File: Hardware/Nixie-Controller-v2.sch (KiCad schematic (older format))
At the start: 219 parts, among them J7 12V DC JACK, U1 MAX1771, U10 74HC4067, U11 M41T01, U12 STM32F103C8, U13 OPA180, U14 74HC4067, U15 OPA180, U16 74HC4067, U17 OPA180, U18 74HC4067, U19 OPA180, U2 BH2226, U20 74HC4067, U21 OPA180, U22 74HC4067, U3 74HC595, U4 74HC595, U5 74HC595, U6 SN74LVCC3245A, U7 NCP1117-5.0, U8 NCP1117-3.3, U9 OPA180, Y1 32.768KHz, Y2 16MHz

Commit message: Remove uC external crystal
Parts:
- removed C24, C25: 10pF, Capacitor_SMD:C_0402_1005Metric, symbol Device:C_Small
- removed Y2: 16MHz, Crystal:Crystal_SMD_2016-4Pin_2.0x1.6mm, symbol Device:Crystal_GND24
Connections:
- wire segments 618 -> 608
- no-connect marks 66 -> 68
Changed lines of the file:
@@
 	0    -1   -1   0
 $EndComp
-Wire Wire Line
-	18050 9850 19300 9850
-Wire Wire Line
-	18050 9750 19300 9750
 $Comp
 L Device:R_Small_US R28
@@
 	1    18850 9200
 	-1   0    0    1
-$EndComp
-$Comp
-L power:GND #PWR0131
-U 1 1 6186A334
-P 20000 10350
-F 0 "#PWR0131" H 20000 10100 50  0001 C CNN
-F 1 "GND" H 20000 10200 50  0000 C CNN
-F 2 "" H 20000 10350 50  0001 C CNN
-F 3 "" H 20000 10350 50  0001 C CNN
-	1    20000 10350
-	1    0    0    -1
-$EndComp
-$Comp
-L power:GND #PWR0125
-U 1 1 61866ACC
-P 20000 9250
-F 0 "#PWR0125" H 20000 9000 50  0001 C CNN
-F 1 "GND" H 20000 9100 50  0000 C CNN
-F 2 "" H 20000 9250 50  0001 C CNN
-F 3 "" H 20000 9250 50  0001 C CNN
-	1    20000 9250
-	-1   0    0    1
-$EndComp
-$Comp
-L power:GND #PWR0129
-U 1 1 618618D6
-P 20200 9800
-F 0 "#PWR0129" H 20200 9550 50  0001 C CNN
-F 1 "GND" V 20200 9650 50  0000 R CNN
-F 2 "" H 20200 9800 50  0001 C CNN
-F 3 "" H 20200 9800 50  0001 C CNN
-	1    20200 9800
-	0    -1   -1   0
-$EndComp
-$Comp
-L power:GND #PWR0128
-U 1 1 6185E39D
-P 19800 9800
-F 0 "#PWR0128" H 19800 9550 50  0001 C CNN
-F 1 "GND" V 19800 9650 50  0000 R CNN
-F 2 "" H 19800 9800 50  0001 C CNN
-F 3 "" H 19800 9800 50  0001 C CNN
-	1    19800 9800
-	0    1    1    0
-$EndComp
-Connection ~ 20000 10050
-Wire Wire Line
-	20000 10050 20000 10150
-Wire Wire Line
-	20000 10050 20000 9950
-Wire Wire Line
-	19300 10050 20000 10050
-Wire Wire Line
-	19300 9850 19300 10050
-Wire Wire Line
-	20000 9550 20000 9650
-Connection ~ 20000 9550
-Wire Wire Line
-	19300 9550 19300 9750
-Wire Wire Line
-	20000 9550 19300 9550
-Wire Wire Line
-	20000 9450 20000 9550
-$Comp
-L Device:C_Small C25
-U 1 1 6169E719
-P 20000 10250
-F 0 "C25" H 20100 10300 50  0000 L CNN
-F 1 "10pF" H 20100 10200 50  0000 L CNN
-F 2 "Capacitor_SMD:C_0402_1005Metric" H 20000 10250 50  0001 C CNN
-F 3 "~" H 20000 10250 50  0001 C CNN
-F 4 "Yageo" H 20000 10250 50  0001 C CNN "Manufacturer"
-F 5 "CC0402CRNPO9BN100" H 20000 10250 50  0001 C CNN "Part#"
-	1    20000 10250
-	1    0    0    -1
-$EndComp
-$Comp
-L Device:C_Small C24
-U 1 1 6169D2AB
-P 20000 9350
-F 0 "C24" H 20100 9400 50  0000 L CNN
-F 1 "10pF" H 20100 9300 50  0000 L CNN
-F 2 "Capacitor_SMD:C_0402_1005Metric" H 20000 9350 50  0001 C CNN
-F 3 "~" H 20000 9350 50  0001 C CNN
-F 4 "Yageo" H 20000 9350 50  0001 C CNN "Manufacturer"
-F 5 "CC0402CRNPO9BN100" H 20000 9350 50  0001 C CNN "Part#"
-	1    20000 9350
-	1    0    0    -1
-$EndComp
-$Comp
-L Device:Crystal_GND24 Y2
-U 1 1 6163FF36
-P 20000 9800
-F 0 "Y2" V 19750 10000 50  0000 L CNN
-F 1 "16MHz" V 19850 9900 50  0000 L CNN
-F 2 "Crystal:Crystal_SMD_2016-4Pin_2.0x1.6mm" H 20000 9800 50  0001 C CNN
-F 3 "~" H 20000 9800 50  0001 C CNN
-F 4 "ECS" H 20000 9800 50  0001 C CNN "Manufacturer"
-F 5 "ECS-160-8-37-CWY-TR" H 20000 9800 50  0001 C CNN "Part#"
-	1    20000 9800
-	0    1    1    0
 $EndComp
 Wire Wire Line
@@
 	1    0    0    -1
 $EndComp
+NoConn ~ 18050 9750
+NoConn ~ 18050 9850
 $EndSCHEMATC

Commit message: Fix Q2~Q61 footprint (schematic only)
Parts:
- removed Q10, Q11, Q12, Q13, Q14, Q15, Q16, Q17, Q18, Q19, Q2, Q20, Q21, Q22, Q23, Q24, Q25, Q26, Q27, Q28, Q29, Q3, Q30, Q31, Q32, Q33, Q34, Q35, Q36, Q37, Q38, Q39, Q4, Q40, Q41, Q42, Q43, Q44, Q45, Q46, Q47, Q48, Q49, Q5, Q50, Q51, Q52, Q53, Q54, Q55, Q56, Q57, Q58, Q59, Q6, Q60, Q61, Q7, Q8, Q9: ~, Package_TO_SOT_SMD:SOT-23, symbol Device:Q_NPN_EBC
- added Q10, Q11, Q12, Q13, Q14, Q15, Q16, Q17, Q18, Q19, Q2, Q20, Q21, Q22, Q23, Q24, Q25, Q26, Q27, Q28, Q29, Q3, Q30, Q31, Q32, Q33, Q34, Q35, Q36, Q37, Q38, Q39, Q4, Q40, Q41, Q42, Q43, Q44, Q45, Q46, Q47, Q48, Q49, Q5, Q50, Q51, Q52, Q53, Q54, Q55, Q56, Q57, Q58, Q59, Q6, Q60, Q61, Q7, Q8, Q9: ~, Package_TO_SOT_SMD:SOT-23, symbol Device:Q_NPN_BEC

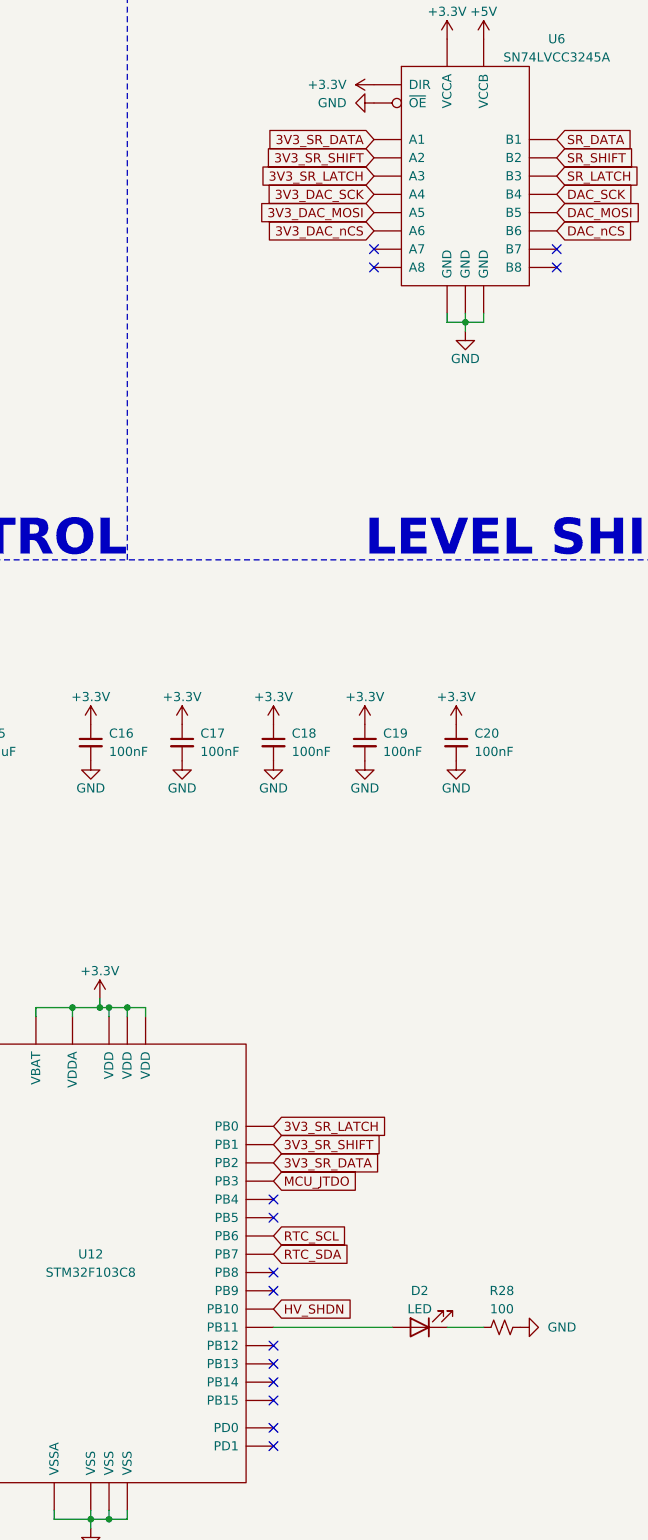
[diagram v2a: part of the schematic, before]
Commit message: Connect shift register to SPI ports
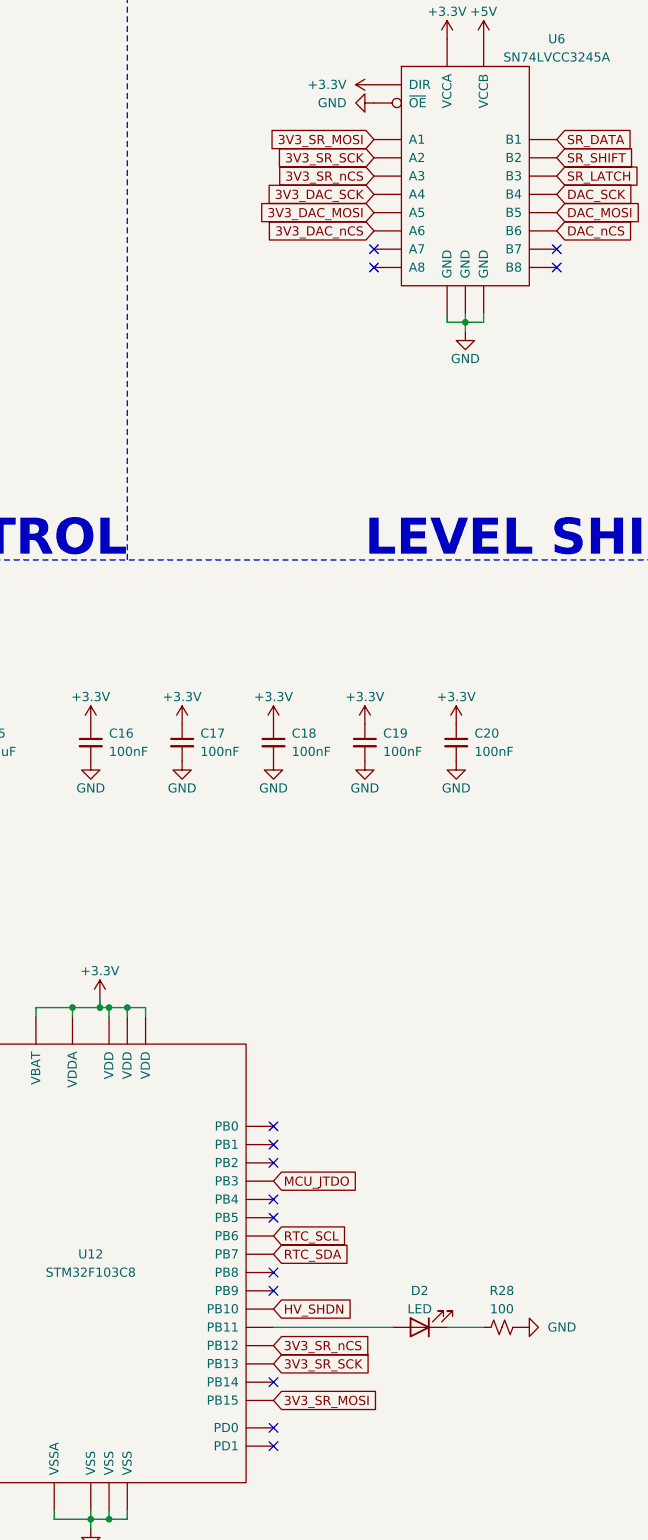
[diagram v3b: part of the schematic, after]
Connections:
- net 3V3_SR_nCS: now reaches U12.25 (PB12)
- net 3V3_SR_nCS: now also U6.5 (A3)
- net 3V3_SR_SCK: now reaches U12.26 (PB13)
- net 3V3_SR_SCK: now also U6.4 (A2)
- net 3V3_SR_MOSI: now reaches U12.28 (PB15)
- net 3V3_SR_MOSI: now also U6.3 (A1)
- net 3V3_SR_DATA: no longer names the net of U12.20 (PB2)
- net 3V3_SR_DATA: no longer U6.3 (A1)
- net 3V3_SR_LATCH: no longer names the net of U12.18 (PB0)
- net 3V3_SR_LATCH: no longer U6.5 (A3)
- net 3V3_SR_SHIFT: no longer names the net of U12.19 (PB1)
- net 3V3_SR_SHIFT: no longer U6.4 (A2)
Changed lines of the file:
@@
 	1    0    0    -1
 $EndComp
-Text GLabel 18600 2800 0    50   Input ~ 0
-3V3_SR_SHIFT
-Text GLabel 18600 2900 0    50   Input ~ 0
-3V3_SR_LATCH
-Text GLabel 18600 2700 0    50   Input ~ 0
-3V3_SR_DATA
 Text GLabel 18600 3000 0    50   Input ~ 0
 3V3_DAC_SCK
@@
 Text GLabel 16050 7900 0    50   Input ~ 0
 MCU_nRST
-$Comp
-L Nixie-Controller-v2:STM32F103C8 U12
-U 1 1 6163BD96
-P 17050 8850
-F 0 "U12" H 17050 8900 50  0000 C CNN
-F 1 "STM32F103C8" H 17050 8800 50  0000 C CNN
-F 2 "Package_QFP:LQFP-48_7x7mm_P0.5mm" H 17050 8900 50  0001 C CNN
-F 3 "~" H 17050 8900 50  0001 C CNN
-F 4 "ST Micro" H 17050 8850 50  0001 C CNN "Manufacturer"
-F 5 "STM32F103C8T6" H 17050 8850 50  0001 C CNN "Part#"
-	1    17050 8850
-	1    0    0    -1
-$EndComp
 Text GLabel 16050 8500 0    50   Input ~ 0
 3V3_DAC_nCS
@@
 Text GLabel 16050 8600 0    50   Input ~ 0
 3V3_DAC_SCK
-Text GLabel 18050 8300 2    50   Input ~ 0
-3V3_SR_DATA
-Text GLabel 18050 8100 2    50   Input ~ 0
-3V3_SR_LATCH
-Text GLabel 18050 8200 2    50   Input ~ 0
-3V3_SR_SHIFT
+Text GLabel 18050 9600 2    50   Input ~ 0
+3V3_SR_MOSI
+Text GLabel 18050 9300 2    50   Input ~ 0
+3V3_SR_nCS
+Text GLabel 18050 9400 2    50   Input ~ 0
+3V3_SR_SCK
 Text GLabel 18050 9100 2    50   Input ~ 0
 HV_SHDN
@@
 NoConn ~ 16050 9850
 NoConn ~ 16050 9950
-NoConn ~ 18050 9600
 NoConn ~ 18050 9500
-NoConn ~ 18050 9400
-NoConn ~ 18050 9300
 NoConn ~ 18050 9000
 NoConn ~ 18050 8900
@@
 	1    0    0    -1
 $EndComp
+Text GLabel 18600 2700 0    50   Input ~ 0
+3V3_SR_MOSI
+Text GLabel 18600 2900 0    50   Input ~ 0
+3V3_SR_nCS
+Text GLabel 18600 2800 0    50   Input ~ 0
+3V3_SR_SCK
+$Comp
+L Nixie-Controller-v2:STM32F103C8 U12
+U 1 1 6163BD96
+P 17050 8850
+F 0 "U12" H 17050 8900 50  0000 C CNN
+F 1 "STM32F103C8" H 17050 8800 50  0000 C CNN
+F 2 "Package_QFP:LQFP-48_7x7mm_P0.5mm" H 17050 8900 50  0001 C CNN
+F 3 "~" H 17050 8900 50  0001 C CNN
+F 4 "ST Micro" H 17050 8850 50  0001 C CNN "Manufacturer"
+F 5 "STM32F103C8T6" H 17050 8850 50  0001 C CNN "Part#"
+	1    17050 8850
+	1    0    0    -1
+$EndComp
+NoConn ~ 18050 8100
+NoConn ~ 18050 8200
+NoConn ~ 18050 8300
 $EndSCHEMATC

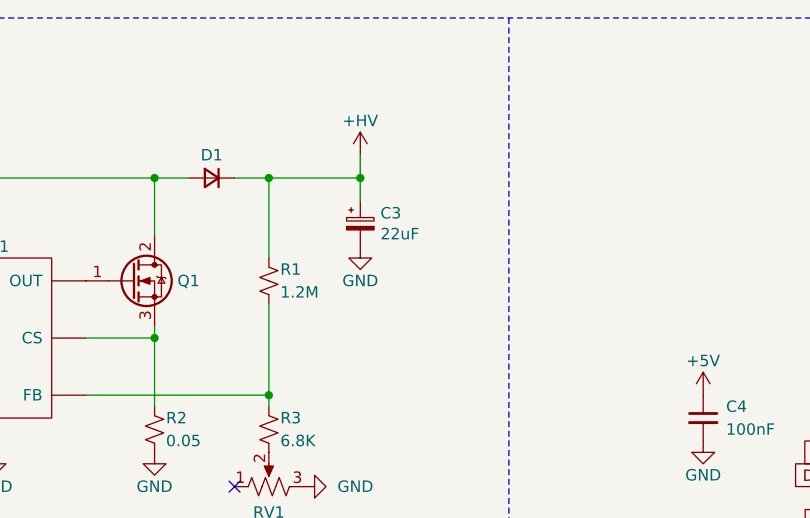
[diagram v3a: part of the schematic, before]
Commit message: Switch HV output cap to 10uF
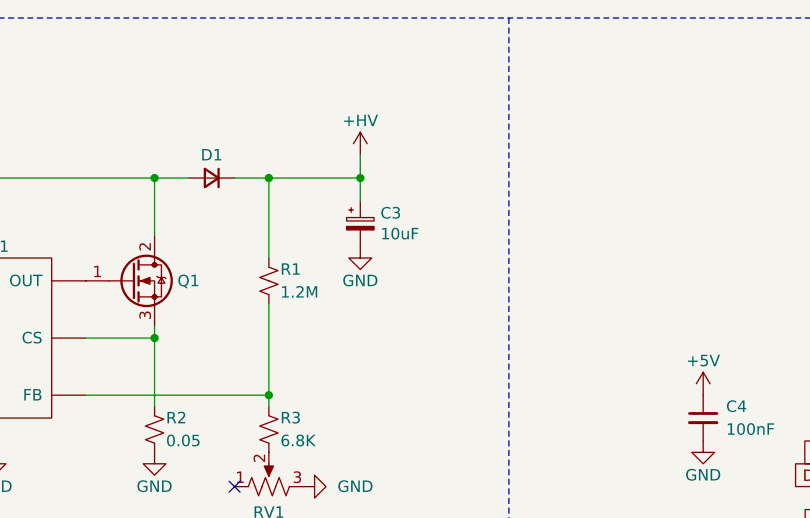
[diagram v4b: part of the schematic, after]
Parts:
- C3: value 22uF -> 10uF; footprint Capacitor_SMD:CP_Elec_18x17.5 -> Capacitor_SMD:CP_Elec_10x10; Part# UUJ2E220MNQ1MS -> UUX2E100MNL1GS
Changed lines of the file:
@@
 P 4350 1400
 F 0 "C3" H 4438 1446 50  0000 L CNN
-F 1 "22uF" H 4438 1355 50  0000 L CNN
-F 2 "Capacitor_SMD:CP_Elec_18x17.5" H 4350 1400 50  0001 C CNN
+F 1 "10uF" H 4438 1355 50  0000 L CNN
+F 2 "Capacitor_SMD:CP_Elec_10x10" H 4350 1400 50  0001 C CNN
 F 3 "~" H 4350 1400 50  0001 C CNN
 F 4 "Nichicon" H 4350 1400 50  0001 C CNN "Manufacturer"
-F 5 "UUJ2E220MNQ1MS" H 4350 1400 50  0001 C CNN "Part#"
+F 5 "UUX2E100MNL1GS" H 4350 1400 50  0001 C CNN "Part#"
 	1    4350 1400
 	1    0    0    -1

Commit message: Add ESP WiFi module
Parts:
- added A1: ESP-12F, RF_Module:ESP-12E, symbol Nixie-Controller-v2:ESP-12F
- added C24: 47uF, Capacitor_SMD:CP_Elec_5x5.3, symbol Device:CP_Small
- added TP17: TX, TestPoint:TestPoint_Pad_D2.5mm, symbol Connector:TestPoint
- added TP18: RX, TestPoint:TestPoint_Pad_D2.5mm, symbol Connector:TestPoint
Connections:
- net +3V3: now also A1.17 (GPIO2), A1.3 (EN), A1.8 (VCC), C24.1
- net GND: now also A1.15 (GND), A1.16 (GPIO15), C24.2
- net ESP_nRST: now reaches U12.10 (PA0)
- net ESP_nRST: now also A1.1 (~RST)
- net ESP_RUN: now reaches U12.11 (PA1)
- net ESP_RUN: now also A1.18 (GPIO0)
- net ESP_TX: now reaches U12.12 (PA2)
- net ESP_TX: now also A1.21 (RX), TP18.1
- net ESP_RX: now reaches U12.13 (PA3)
- net ESP_RX: now also A1.22 (TX), TP17.1
- no-connect marks 68 -> 77
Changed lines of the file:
@@
 F 1 "M41T01" H 24250 8774 50  0000 C CNN
 F 2 "Package_SO:SOIC-8_3.9x4.9mm_P1.27mm" H 24250 8850 50  0001 C CNN
-F 3 "" H 24250 8850 50  0001 C CNN
+F 3 "~" H 24250 8850 50  0001 C CNN
 F 4 "ST Micro" H 24250 8450 50  0001 C CNN "Manufacturer"
 F 5 "M41T01M6F" H 24250 8450 50  0001 C CNN "Part#"
@@
 Text Notes 27850 11400 2    197  ~ 39
 REAL TIME CLOCK
-Wire Notes Line width 20
-	14500 11400 27850 11400
-Wire Notes Line width 20
-	32600 500  32600 5000
 $Comp
 L Device:Battery_Cell BT1
@@
 	1    0    0    -1
 $EndComp
-NoConn ~ 16050 8100
-NoConn ~ 16050 8200
-NoConn ~ 16050 8300
-NoConn ~ 16050 8400
 NoConn ~ 16050 8900
 NoConn ~ 16050 8700
@@
 NoConn ~ 18050 8200
 NoConn ~ 18050 8300
+$Comp
+L Nixie-Controller-v2:ESP-12F A1
+U 1 1 61812F32
+P 30400 8400
+F 0 "A1" H 30400 9015 50  0000 C CNN
+F 1 "ESP-12F" H 30400 8924 50  0000 C CNN
+F 2 "RF_Module:ESP-12E" H 30400 9000 50  0001 C CNN
+F 3 "~" H 30400 9000 50  0001 C CNN
+F 4 "Adafruit" H 30400 8400 50  0001 C CNN "Manufacturer"
+F 5 "2491" H 30400 8400 50  0001 C CNN "Part#"
+	1    30400 8400
+	1    0    0    -1
+$EndComp
+Text GLabel 29650 8050 0    50   Input ~ 0
+ESP_nRST
+Text GLabel 31150 8150 2    50   Input ~ 0
+ESP_TX
+Text GLabel 31150 8050 2    50   Input ~ 0
+ESP_RX
+$Comp
+L power:+3.3V #PWR0216
+U 1 1 618226D2
+P 29650 8750
+F 0 "#PWR0216" H 29650 8600 50  0001 C CNN
+F 1 "+3.3V" V 29650 8900 50  0000 L CNN
+F 2 "" H 29650 8750 50  0001 C CNN
+F 3 "" H 29650 8750 50  0001 C CNN
+	1    29650 8750
+	0    -1   -1   0
+$EndComp
+$Comp
+L power:+3.3V #PWR0129
+U 1 1 618294E9
+P 29650 8250
+F 0 "#PWR0129" H 29650 8100 50  0001 C CNN
+F 1 "+3.3V" V 29650 8400 50  0000 L CNN
+F 2 "" H 29650 8250 50  0001 C CNN
+F 3 "" H 29650 8250 50  0001 C CNN
+	1    29650 8250
+	0    -1   -1   0
+$EndComp
+Text GLabel 31150 8450 2    50   Input ~ 0
+ESP_RUN
+$Comp
+L power:GND #PWR0217
+U 1 1 61889434
+P 31200 8800
+F 0 "#PWR0217" H 31200 8550 50  0001 C CNN
+F 1 "GND" H 31200 8650 50  0000 C CNN
+F 2 "" H 31200 8800 50  0001 C CNN
+F 3 "" H 31200 8800 50  0001 C CNN
+	1    31200 8800
+	1    0    0    -1
+$EndComp
+Wire Wire Line
+	31150 8750 31200 8750
+Wire Wire Line
+	31200 8750 31200 8800
+Wire Wire Line
+	31150 8650 31200 8650
+Wire Wire Line
+	31200 8650 31200 8750
+Connection ~ 31200 8750
+$Comp
+L power:+3.3V #PWR0131
+U 1 1 61949ABC
+P 31150 8550
+F 0 "#PWR0131" H 31150 8400 50  0001 C CNN
+F 1 "+3.3V" V 31150 8700 50  0000 L CNN
+F 2 "" H 31150 8550 50  0001 C CNN
+F 3 "" H 31150 8550 50  0001 C CNN
+	1    31150 8550
+	0    1    1    0
+$EndComp
+NoConn ~ 31150 8250
+NoConn ~ 31150 8350
+NoConn ~ 29650 8150
+NoConn ~ 29650 8350
+NoConn ~ 29650 8450
+NoConn ~ 29650 8550
+NoConn ~ 29650 8650
+NoConn ~ 30150 9150
+NoConn ~ 30250 9150
+NoConn ~ 30350 9150
+NoConn ~ 30450 9150
+NoConn ~ 30550 9150
+NoConn ~ 30650 9150
+$Comp
+L Connector:TestPoint TP17
+U 1 1 61DEE128
+P 30900 6950
+F 0 "TP17" V 30850 7150 50  0000 L CNN
+F 1 "TX" V 30950 7150 50  0000 L CNN
+F 2 "TestPoint:TestPoint_Pad_D2.5mm" H 31100 6950 50  0001 C CNN
+F 3 "~" H 31100 6950 50  0001 C CNN
+F 4 "~" H 30900 6950 50  0001 C CNN "Manufacturer"
+F 5 "~" H 30900 6950 50  0001 C CNN "Part#"
+	1    30900 6950
+	0    1    1    0
+$EndComp
+$Comp
+L Connector:TestPoint TP18
+U 1 1 61E4963F
+P 30900 7200
+F 0 "TP18" V 30850 7400 50  0000 L CNN
+F 1 "RX" V 30950 7400 50  0000 L CNN
+F 2 "TestPoint:TestPoint_Pad_D2.5mm" H 31100 7200 50  0001 C CNN
+F 3 "~" H 31100 7200 50  0001 C CNN
+F 4 "~" H 30900 7200 50  0001 C CNN "Manufacturer"
+F 5 "~" H 30900 7200 50  0001 C CNN "Part#"
+	1    30900 7200
+	0    1    1    0
+$EndComp
+$Comp
+L Device:CP_Small C24
+U 1 1 61EA48C6
+P 29600 7050
+F 0 "C24" H 29700 7100 50  0000 L CNN
+F 1 "47uF" H 29700 7000 50  0000 L CNN
+F 2 "Capacitor_SMD:CP_Elec_5x5.3" H 29600 7050 50  0001 C CNN
+F 3 "~" H 29600 7050 50  0001 C CNN
+F 4 "Nichicon" H 29600 7050 50  0001 C CNN "Manufacturer"
+F 5 "UWF0J470MCL1GB" H 29600 7050 50  0001 C CNN "Part#"
+	1    29600 7050
+	1    0    0    -1
+$EndComp
+$Comp
+L power:GND #PWR0128
+U 1 1 61EA9391
+P 29600 7150
+F 0 "#PWR0128" H 29600 6900 50  0001 C CNN
+F 1 "GND" H 29600 7000 50  0000 C CNN
+F 2 "" H 29600 7150 50  0001 C CNN
+F 3 "" H 29600 7150 50  0001 C CNN
+	1    29600 7150
+	1    0    0    -1
+$EndComp
+$Comp
+L power:+3.3V #PWR0125
+U 1 1 61F072D5
+P 29600 6950
+F 0 "#PWR0125" H 29600 6800 50  0001 C CNN
+F 1 "+3.3V" H 29600 7100 50  0000 C CNN
+F 2 "" H 29600 6950 50  0001 C CNN
+F 3 "" H 29600 6950 50  0001 C CNN
+	1    29600 6950
+	1    0    0    -1
+$EndComp
+Text GLabel 30900 7200 0    50   Input ~ 0
+ESP_TX
+Text GLabel 30900 6950 0    50   Input ~ 0
+ESP_RX
+Text GLabel 16050 8100 0    50   Input ~ 0
+ESP_nRST
+Wire Notes Line width 20
+	14500 11400 32600 11400
+Wire Notes Line width 20
+	32600 500  32600 11400
+Text GLabel 16050 8300 0    50   Input ~ 0
+ESP_TX
+Text GLabel 16050 8400 0    50   Input ~ 0
+ESP_RX
+Text GLabel 16050 8200 0    50   Input ~ 0
+ESP_RUN
 $EndSCHEMATC

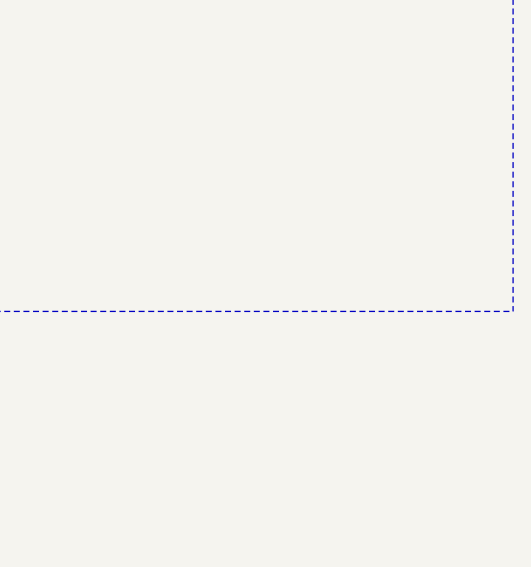
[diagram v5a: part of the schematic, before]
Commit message: Add WiFi section label to schematic
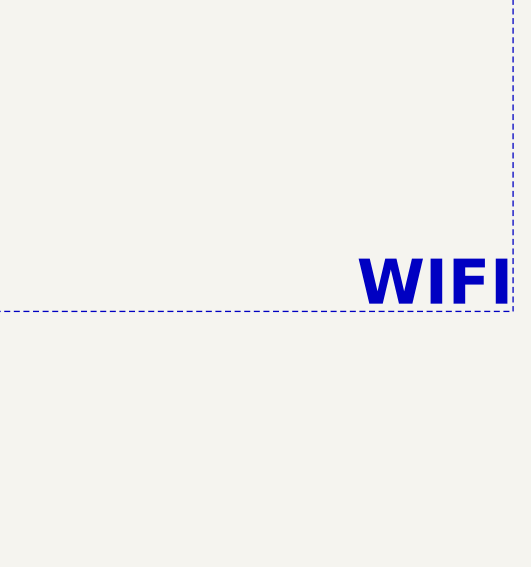
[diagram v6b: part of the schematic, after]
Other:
- note added: "WIFI"
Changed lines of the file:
@@
 Text GLabel 16050 8200 0    50   Input ~ 0
 ESP_RUN
+Text Notes 32600 11400 2    197  ~ 39
+WIFI
 $EndSCHEMATC

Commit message: Remove status LED
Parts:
- removed D2: LED, Diode_SMD:D_0603_1608Metric, symbol Device:LED
- removed R28: 100, Resistor_SMD:R_0402_1005Metric, symbol Device:R_Small_US
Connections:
- no-connect marks 77 -> 78
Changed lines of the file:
@@
-$EndComp
-Wire Wire Line
-	18700 9200 18050 9200
-Wire Wire Line
-	19200 9200 19000 9200
-$Comp
-L power:GND #PWR0124
-U 1 1 61A95A14
-P 19400 9200
-F 0 "#PWR0124" H 19400 8950 50  0001 C CNN
-F 1 "GND" V 19400 9050 50  0000 R CNN
-F 2 "" H 19400 9200 50  0001 C CNN
-F 3 "" H 19400 9200 50  0001 C CNN
-	1    19400 9200
-	0    -1   -1   0
-$EndComp
-$Comp
-L Device:R_Small_US R28
-U 1 1 6186EA54
-P 19300 9200
-F 0 "R28" V 19100 9200 50  0000 C CNN
-F 1 "100" V 19200 9200 50  0000 C CNN
-F 2 "Resistor_SMD:R_0402_1005Metric" H 19300 9200 50  0001 C CNN
-F 3 "~" H 19300 9200 50  0001 C CNN
-F 4 "Yageo" H 19300 9200 50  0001 C CNN "Manufacturer"
-F 5 "RC0402FR-07100RL" H 19300 9200 50  0001 C CNN "Part#"
-	1    19300 9200
-	0    1    1    0
-$EndComp
-$Comp
-L Device:LED D2
-U 1 1 6186BE38
-P 18850 9200
-F 0 "D2" H 18850 9000 50  0000 C CNN
-F 1 "LED" H 18850 9100 50  0000 C CNN
-F 2 "Diode_SMD:D_0603_1608Metric" H 18850 9200 50  0001 C CNN
-F 3 "~" H 18850 9200 50  0001 C CNN
-F 4 "Rohm Semi" H 18850 9200 50  0001 C CNN "Manufacturer"
-F 5 "SML-D12U1WT86" H 18850 9200 50  0001 C CNN "Part#"
-	1    18850 9200
-	-1   0    0    1
 $EndComp
 Wire Wire Line
@@
 Text Notes 32600 11400 2    197  ~ 39
 WIFI
+NoConn ~ 18050 9200
 $EndSCHEMATC
